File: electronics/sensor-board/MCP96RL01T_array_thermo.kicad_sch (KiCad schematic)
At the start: 75 parts, among them J23 Therm_1, J24 Therm_4, J25 Therm_7, J26 Therm_2, J27 Therm_5, J28 Therm_3, J29 Therm_6, U10 MCP96RL01T, U4 MCP96RL01T, U5 MCP96RL01T, U6 MCP96RL01T, U7 MCP96RL01T, U8 MCP96RL01T, U9 MCP96RL01T

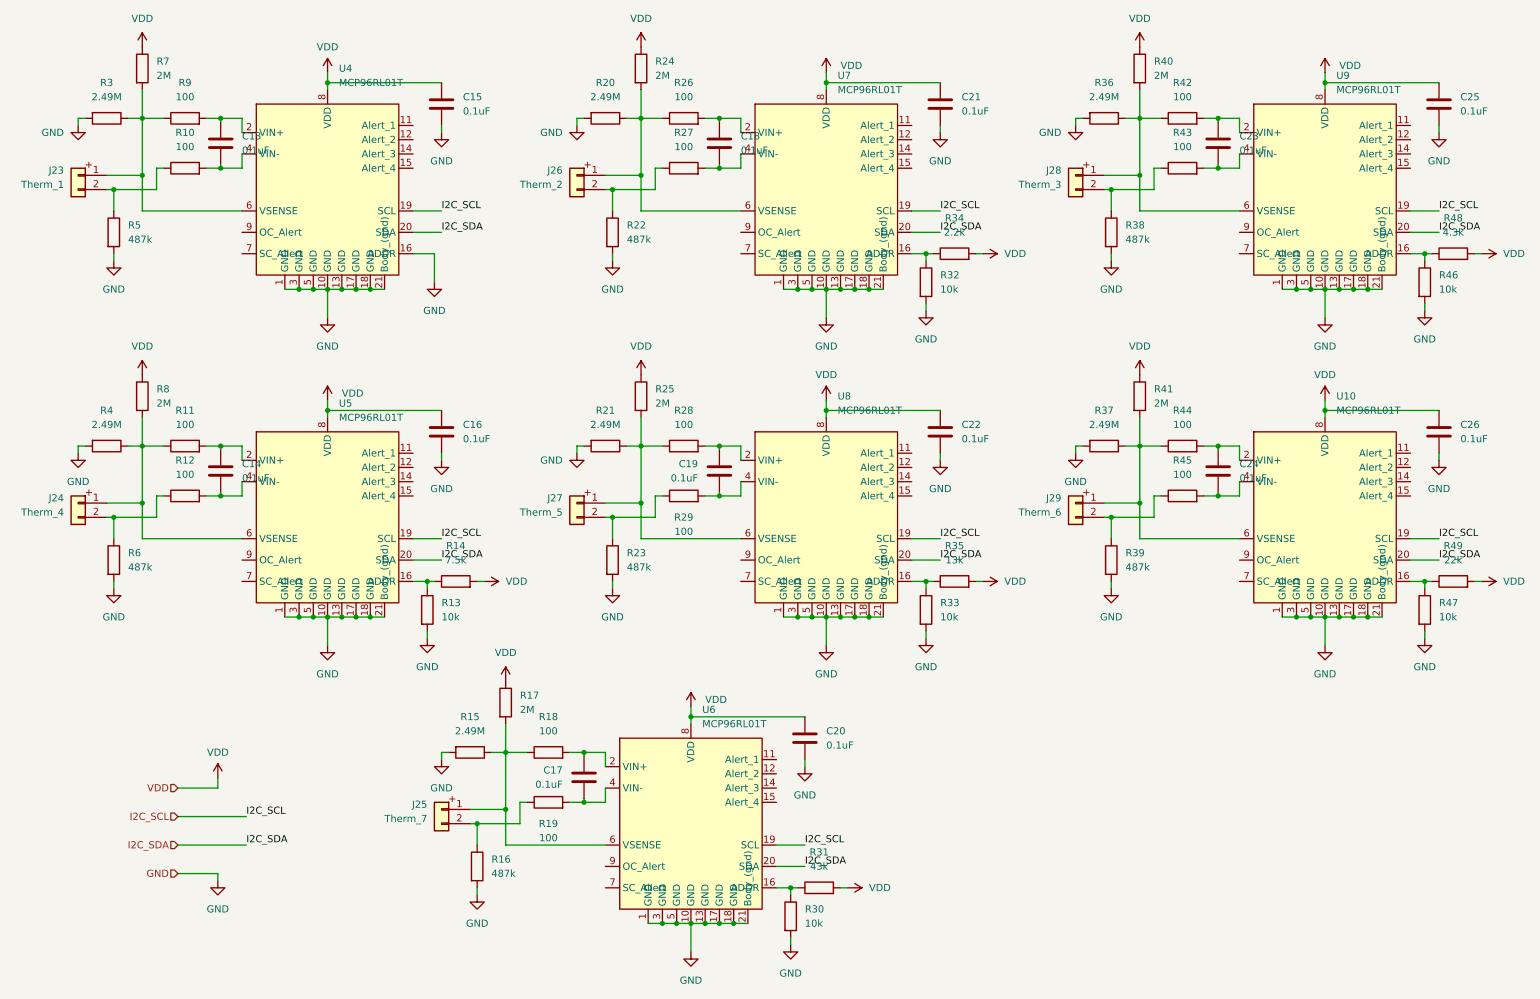
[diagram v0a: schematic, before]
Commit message: updated loadcell amplifier
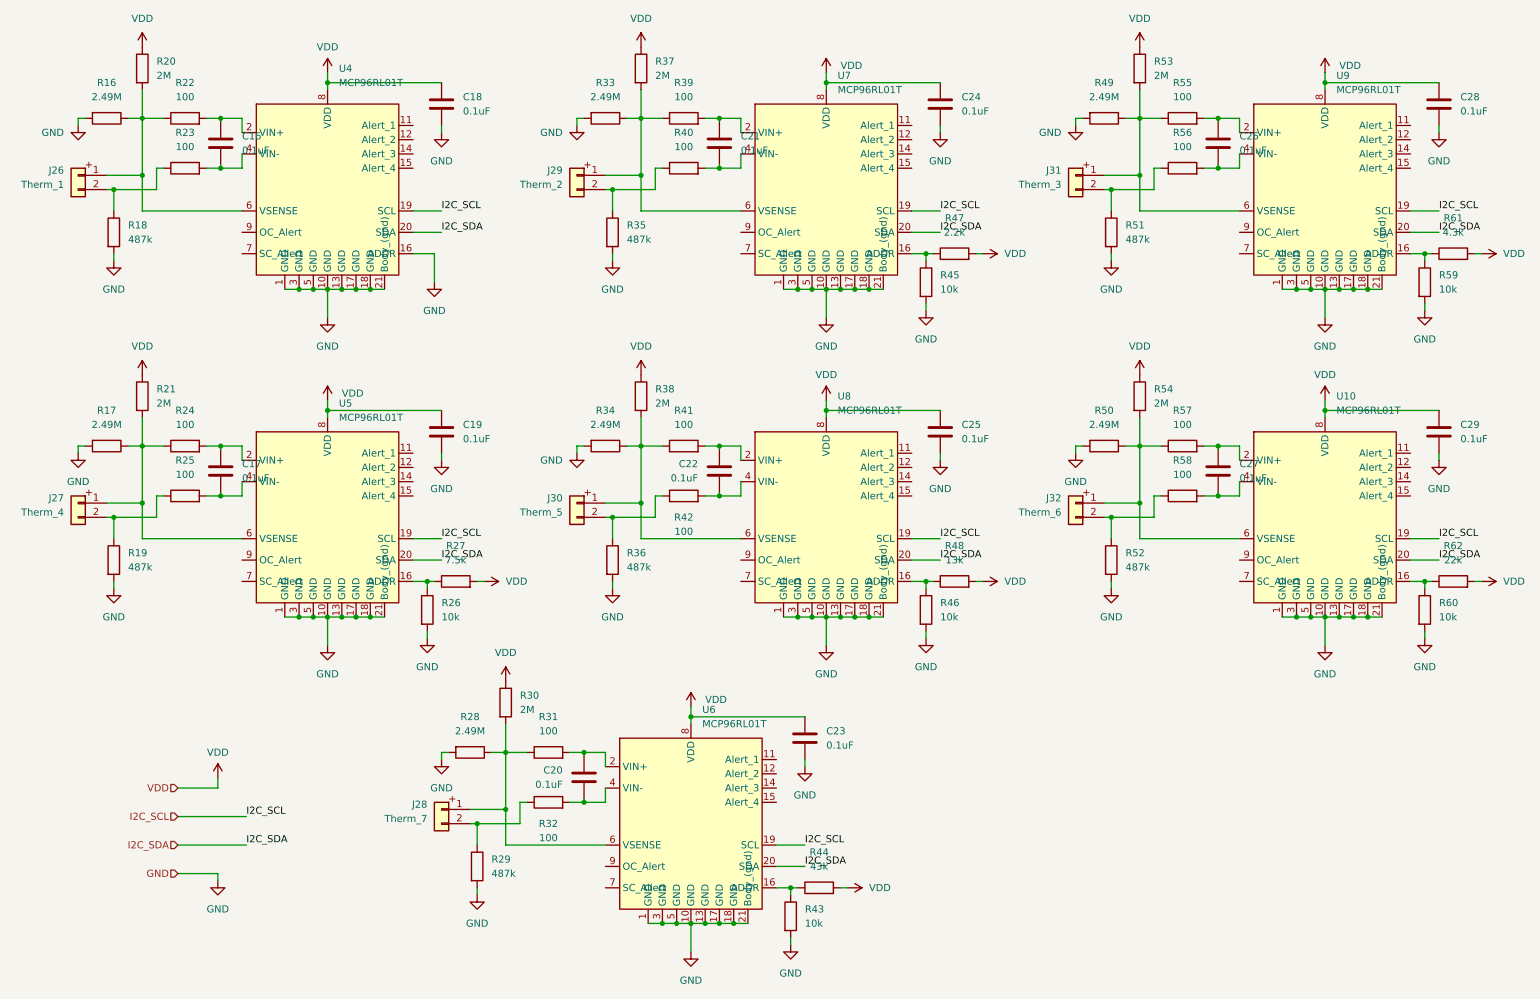
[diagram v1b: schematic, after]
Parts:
- renumbered C13 to C16, C14 to C17, C15 to C18, C16 to C19, C17 to C20, C18 to C21, C19 to C22, C20 to C23, C21 to C24, C22 to C25, C23 to C26, C24 to C27, C25 to C28, C26 to C29, J23 to J26, J24 to J27, J25 to J28, J26 to J29, J27 to J30, J28 to J31, J29 to J32, R3 to R16, R4 to R17, R5 to R18, R6 to R19, R7 to R20, R8 to R21, R9 to R22, R10 to R23, R11 to R24, R12 to R25, R13 to R26, R14 to R27, R15 to R28, R16 to R29, R17 to R30, R18 to R31, R19 to R32, R20 to R33, R21 to R34, R22 to R35, R23 to R36, R24 to R37, R25 to R38, R26 to R39, R27 to R40, R28 to R41, R29 to R42, R30 to R43, R31 to R44, R32 to R45, R33 to R46, R34 to R47, R35 to R48, R36 to R49, R37 to R50, R38 to R51, R39 to R52, R40 to R53, R41 to R54, R42 to R55, R43 to R56, R44 to R57, R45 to R58, R46 to R59, R47 to R60, R48 to R61, R49 to R62
